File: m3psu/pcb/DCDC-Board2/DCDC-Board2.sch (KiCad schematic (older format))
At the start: 6 parts

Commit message: Start DC/DC routing
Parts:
- gave numbers to parts that had none: 6
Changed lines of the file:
@@
 EESchema Schematic File Version 2
 LIBS:agg-kicad
-LIBS:m3psu-cache
 EELAYER 25 0
 EELAYER END
 $Descr A4 11693 8268
 encoding utf-8
-Sheet 8 13
+Sheet 1 3
 Title ""
 Date ""
@@
 ~ALERT
 $Comp
-L GND #PWR?
+L GND #PWR01
 U 1 1 56E23B16
 P 9150 1700
-F 0 "#PWR?" H 9020 1740 50  0001 L CNN
+F 0 "#PWR01" H 9020 1740 50  0001 L CNN
 F 1 "GND" H 9150 1600 50  0000 C CNN
 F 2 "" H 9150 1700 60  0000 C CNN
@@
 $EndComp
 $Comp
-L GND #PWR?
+L GND #PWR02
 U 1 1 56E23B1C
 P 8750 1700
-F 0 "#PWR?" H 8620 1740 50  0001 L CNN
+F 0 "#PWR02" H 8620 1740 50  0001 L CNN
 F 1 "GND" H 8750 1600 50  0000 C CNN
 F 2 "" H 8750 1700 60  0000 C CNN
@@
 $EndComp
 $Comp
-L GND #PWR?
+L GND #PWR03
 U 1 1 56E23B22
 P 8750 700
-F 0 "#PWR?" H 8620 740 50  0001 L CNN
+F 0 "#PWR03" H 8620 740 50  0001 L CNN
 F 1 "GND" H 8750 600 50  0000 C CNN
 F 2 "" H 8750 700 60  0000 C CNN
@@
 $EndComp
 $Comp
-L GND #PWR?
+L GND #PWR04
 U 1 1 56E23B28
 P 9150 700
-F 0 "#PWR?" H 9020 740 50  0001 L CNN
+F 0 "#PWR04" H 9020 740 50  0001 L CNN
 F 1 "GND" H 9150 600 50  0000 C CNN
 F 2 "" H 9150 700 60  0000 C CNN
@@
 $EndComp
 $Comp
-L GND #PWR?
+L GND #PWR05
 U 1 1 56E23B2E
 P 10150 1700
-F 0 "#PWR?" H 10020 1740 50  0001 L CNN
+F 0 "#PWR05" H 10020 1740 50  0001 L CNN
 F 1 "GND" H 10150 1600 50  0000 C CNN
 F 2 "" H 10150 1700 60  0000 C CNN
@@
 $EndComp
 $Comp
-L GND #PWR?
+L GND #PWR06
 U 1 1 56E23B34
 P 10550 1700
-F 0 "#PWR?" H 10420 1740 50  0001 L CNN
+F 0 "#PWR06" H 10420 1740 50  0001 L CNN
 F 1 "GND" H 10550 1600 50  0000 C CNN
 F 2 "" H 10550 1700 60  0000 C CNN
@@
 $EndComp
 $Comp
-L GND #PWR?
+L GND #PWR07
 U 1 1 56E23B3A
 P 10150 700
-F 0 "#PWR?" H 10020 740 50  0001 L CNN
+F 0 "#PWR07" H 10020 740 50  0001 L CNN
 F 1 "GND" H 10150 600 50  0000 C CNN
 F 2 "" H 10150 700 60  0000 C CNN
@@
 $EndComp
 $Comp
-L GND #PWR?
+L GND #PWR08
 U 1 1 56E23B40
 P 10550 700
-F 0 "#PWR?" H 10420 740 50  0001 L CNN
+F 0 "#PWR08" H 10420 740 50  0001 L CNN
 F 1 "GND" H 10550 600 50  0000 C CNN
 F 2 "" H 10550 700 60  0000 C CNN
@@
 CAN+
 $Comp
-L GND #PWR?
+L GND #PWR09
 U 1 1 56E23B52
 P 9150 3000
-F 0 "#PWR?" H 9020 3040 50  0001 L CNN
+F 0 "#PWR09" H 9020 3040 50  0001 L CNN
 F 1 "GND" H 9150 2900 50  0000 C CNN
 F 2 "" H 9150 3000 60  0000 C CNN
@@
 $EndComp
 $Comp
-L GND #PWR?
+L GND #PWR010
 U 1 1 56E23B58
 P 8750 3000
-F 0 "#PWR?" H 8620 3040 50  0001 L CNN
+F 0 "#PWR010" H 8620 3040 50  0001 L CNN
 F 1 "GND" H 8750 2900 50  0000 C CNN
 F 2 "" H 8750 3000 60  0000 C CNN
@@
 $EndComp
 $Comp
-L GND #PWR?
+L GND #PWR011
 U 1 1 56E23B5E
 P 8750 2000
-F 0 "#PWR?" H 8620 2040 50  0001 L CNN
+F 0 "#PWR011" H 8620 2040 50  0001 L CNN
 F 1 "GND" H 8750 1900 50  0000 C CNN
 F 2 "" H 8750 2000 60  0000 C CNN
@@
 $EndComp
 $Comp
-L GND #PWR?
+L GND #PWR012
 U 1 1 56E23B64
 P 9150 2000
-F 0 "#PWR?" H 9020 2040 50  0001 L CNN
+F 0 "#PWR012" H 9020 2040 50  0001 L CNN
 F 1 "GND" H 9150 1900 50  0000 C CNN
 F 2 "" H 9150 2000 60  0000 C CNN
@@
 PYRO1
 $Comp
-L GND #PWR?
+L GND #PWR013
 U 1 1 56E23B86
 P 10150 3000
-F 0 "#PWR?" H 10020 3040 50  0001 L CNN
+F 0 "#PWR013" H 10020 3040 50  0001 L CNN
 F 1 "GND" H 10150 2900 50  0000 C CNN
 F 2 "" H 10150 3000 60  0000 C CNN
@@
 $EndComp
 $Comp
-L GND #PWR?
+L GND #PWR014
 U 1 1 56E23B8C
 P 10550 3000
-F 0 "#PWR?" H 10420 3040 50  0001 L CNN
+F 0 "#PWR014" H 10420 3040 50  0001 L CNN
 F 1 "GND" H 10550 2900 50  0000 C CNN
 F 2 "" H 10550 3000 60  0000 C CNN
@@
 $EndComp
 $Comp
-L GND #PWR?
+L GND #PWR015
 U 1 1 56E23B92
 P 10150 2000
-F 0 "#PWR?" H 10020 2040 50  0001 L CNN
+F 0 "#PWR015" H 10020 2040 50  0001 L CNN
 F 1 "GND" H 10150 1900 50  0000 C CNN
 F 2 "" H 10150 2000 60  0000 C CNN
@@
 $EndComp
 $Comp
-L GND #PWR?
+L GND #PWR016
 U 1 1 56E23B98
 P 10550 2000
-F 0 "#PWR?" H 10420 2040 50  0001 L CNN
+F 0 "#PWR016" H 10420 2040 50  0001 L CNN
 F 1 "GND" H 10550 1900 50  0000 C CNN
 F 2 "" H 10550 2000 60  0000 C CNN
@@
 INTERCONNECTS
 $Comp
-L GND #PWR?
+L GND #PWR017
 U 1 1 56E23BAF
 P 9600 4000
-F 0 "#PWR?" H 9470 4040 50  0001 L CNN
+F 0 "#PWR017" H 9470 4040 50  0001 L CNN
 F 1 "GND" H 9600 3900 50  0000 C CNN
 F 2 "" H 9600 4000 60  0000 C CNN
@@
 	8800 1550 8700 1550
 $Comp
-L PWR #FLG?
+L PWR #FLG018
 U 1 1 56E23C21
 P 9600 3950
-F 0 "#FLG?" H 9600 4110 50  0001 C CNN
+F 0 "#FLG018" H 9600 4110 50  0001 C CNN
 F 1 "PWR" H 9600 4040 50  0000 C CNN
 F 2 "" H 9600 3950 50  0001 C CNN
@@
 	9600 3950 9600 4000
 $Comp
-L CONN_02x10 J?
+L CONN_02x10 J1
 U 1 1 56E23C29
 P 9000 750
-F 0 "J?" H 8900 850 50  0000 L CNN
+F 0 "J1" H 8900 850 50  0000 L CNN
 F 1 "WEST TOP" H 8950 -250 50  0000 C CNN
 F 2 "agg:TFML-110-02-L-D" H 9000 750 50  0001 C CNN
@@
 $EndComp
 $Comp
-L CONN_02x10 J?
+L CONN_02x10 J4
 U 1 1 56E23C31
 P 10400 750
-F 0 "J?" H 10300 850 50  0000 L CNN
+F 0 "J4" H 10300 850 50  0000 L CNN
 F 1 "EAST TOP" H 10350 -250 50  0000 C CNN
 F 2 "agg:TFML-110-02-L-D" H 10400 750 50  0001 C CNN
@@
 $EndComp
 $Comp
-L CONN_02x10 J?
+L CONN_02x10 J2
 U 1 1 56E23C39
 P 9000 2050
-F 0 "J?" H 8900 2150 50  0000 L CNN
+F 0 "J2" H 8900 2150 50  0000 L CNN
 F 1 "WEST BOT" H 8950 1050 50  0000 C CNN
 F 2 "agg:SFML-110-02-L-D-LC" H 9000 2050 50  0001 C CNN
@@
 $EndComp
 $Comp
-L CONN_02x10 J?
+L CONN_02x10 J5
 U 1 1 56E23C41
 P 10400 2050
-F 0 "J?" H 10300 2150 50  0000 L CNN
+F 0 "J5" H 10300 2150 50  0000 L CNN
 F 1 "EAST BOT" H 10350 1050 50  0000 C CNN
 F 2 "agg:SFML-110-02-L-D-LC" H 10400 2050 50  0001 C CNN
@@
 $EndComp
 $Comp
-L CONN_02x05 J?
+L CONN_02x05 J3
 U 1 1 56E23C48
 P 9000 3300
-F 0 "J?" H 8900 3400 50  0000 L CNN
+F 0 "J3" H 8900 3400 50  0000 L CNN
 F 1 "NORTH TOP" H 8950 2800 50  0000 C CNN
 F 2 "agg:SFML-105-02-L-D" H 9000 3300 50  0001 C CNN
@@
 ~ALERT
 $Comp
-L CONN_02x05 J?
+L CONN_02x05 J6
 U 1 1 56E23C63
 P 10400 3300
-F 0 "J?" H 10300 3400 50  0000 L CNN
+F 0 "J6" H 10300 3400 50  0000 L CNN
 F 1 "NORTH BOT" H 10350 2800 50  0000 C CNN
 F 2 "agg:SFML-105-02-L-D-LC" H 10400 3300 50  0001 C CNN
@@
 V_MAIN
 $Comp
-L VCC #PWR?
+L VCC #PWR019
 U 1 1 56E23C7F
 P 9050 4050
-F 0 "#PWR?" H 9050 4160 50  0001 L CNN
+F 0 "#PWR019" H 9050 4160 50  0001 L CNN
 F 1 "VCC" V 9000 4150 50  0000 C CNN
 F 2 "" H 9050 4050 60  0000 C CNN
@@
 	8900 4050 9050 4050
 $Comp
-L 3v3 #PWR?
+L 3v3 #PWR020
 U 1 1 56E23C86
 P 10450 4050
-F 0 "#PWR?" H 10450 4160 50  0001 L CNN
+F 0 "#PWR020" H 10450 4160 50  0001 L CNN
 F 1 "3v3" V 10400 4150 50  0000 C CNN
 F 2 "" H 10450 4050 60  0000 C CNN
@@
 3v3_PSU
 $Comp
-L PWR #FLG?
+L PWR #FLG021
 U 1 1 56E23C8E
 P 9000 4000
-F 0 "#FLG?" H 9000 4160 50  0001 C CNN
+F 0 "#FLG021" H 9000 4160 50  0001 C CNN
 F 1 "PWR" H 9000 4090 50  0000 C CNN
 F 2 "" H 9000 4000 50  0001 C CNN
@@
 Connection ~ 9000 4050
 $Comp
-L PWR #FLG?
+L PWR #FLG022
 U 1 1 56E23C96
 P 10400 4000
-F 0 "#FLG?" H 10400 4160 50  0001 C CNN
+F 0 "#FLG022" H 10400 4160 50  0001 C CNN
 F 1 "PWR" H 10400 4090 50  0000 C CNN
 F 2 "" H 10400 4000 50  0001 C CNN

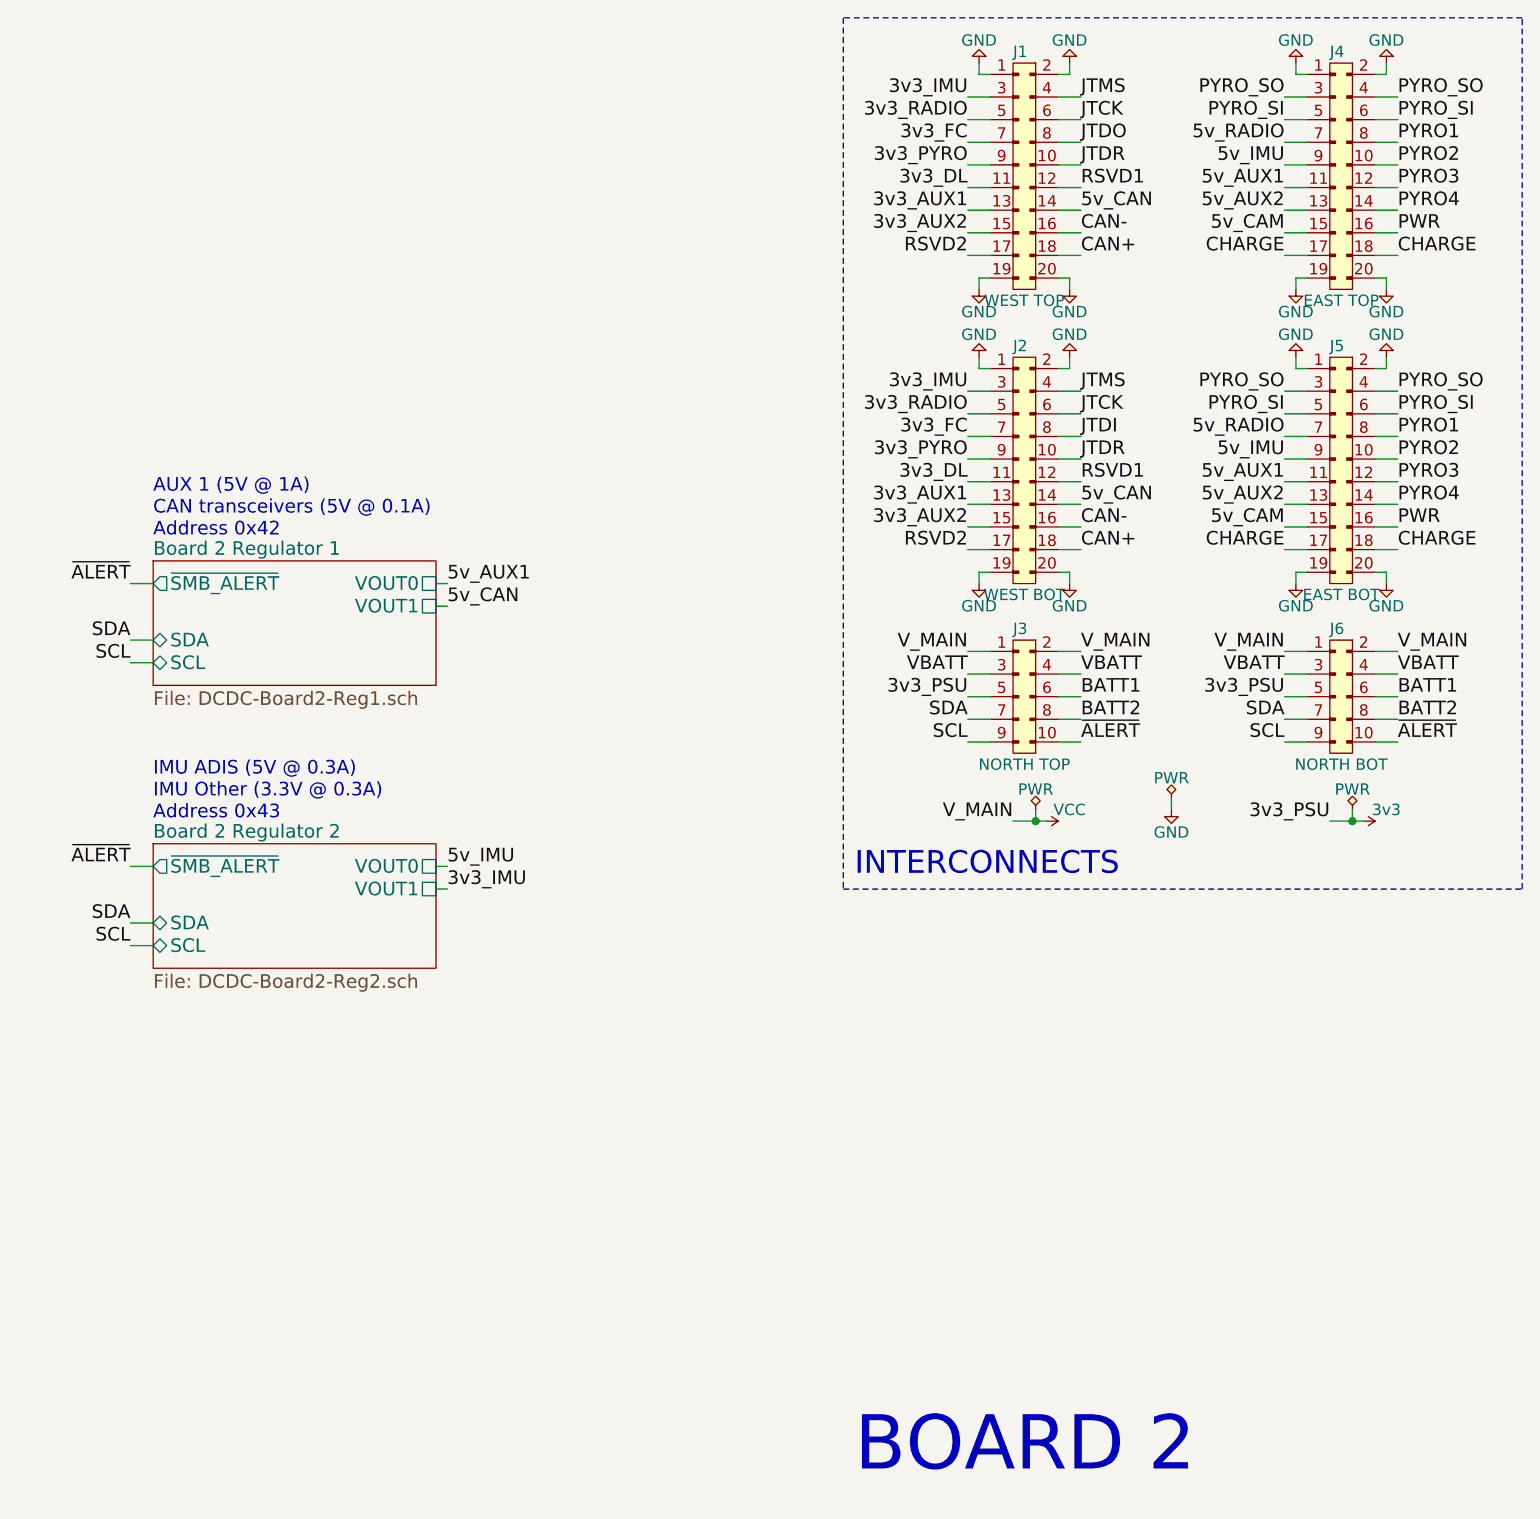
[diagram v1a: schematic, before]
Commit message: Finish routing DC-DC Board 2
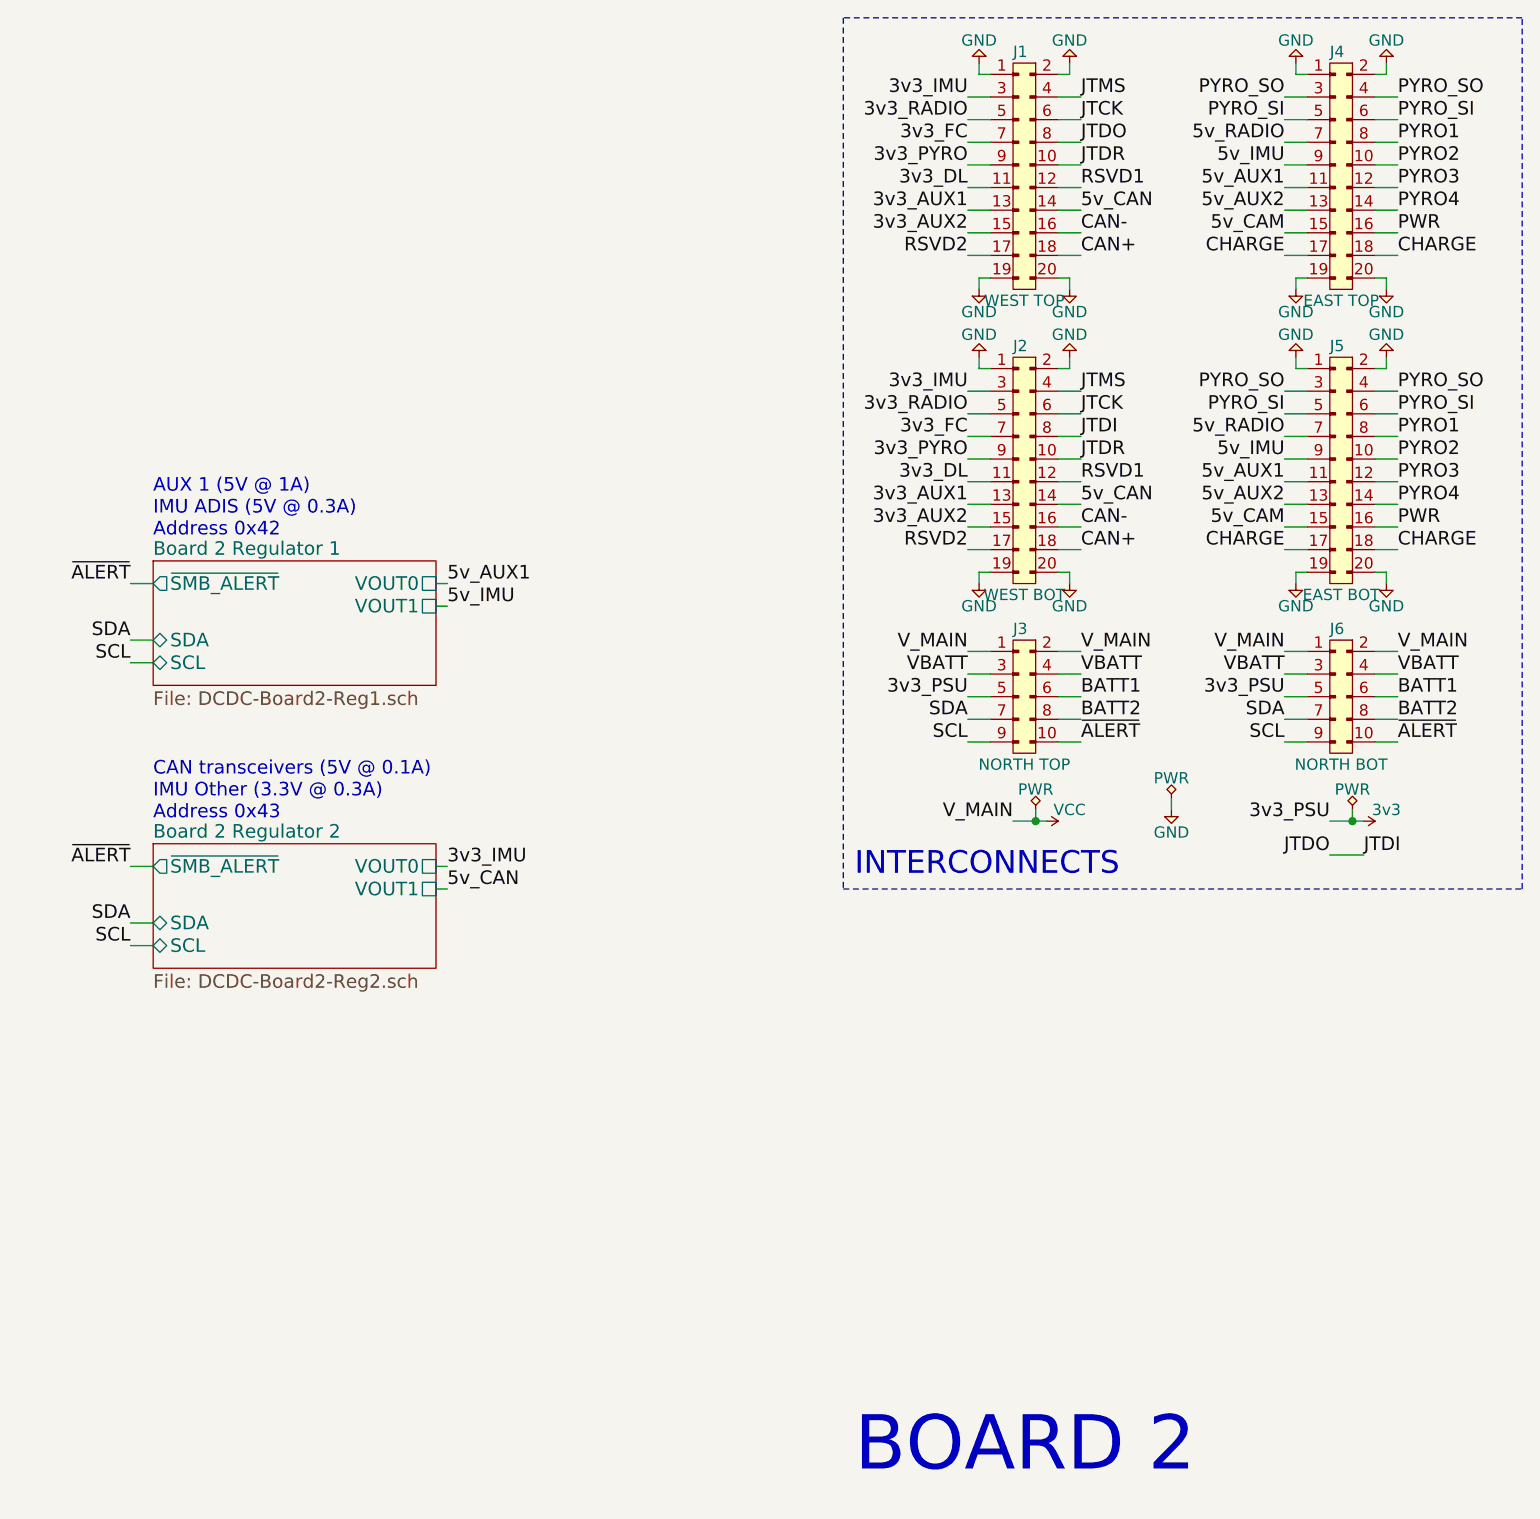
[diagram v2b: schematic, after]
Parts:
- J3: footprint agg:SFML-105-02-L-D -> agg:TFML-105-02-L-D
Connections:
- net JTDO is gone; now on net JTDI: J1.8
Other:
- note added: "AUX 1 (5V @ 1A)\nIMU ADIS (5V @ 0.3A)\nAddress 0x42"
- note added: "CAN transceivers (5V @ 0.1A)\nIMU Other (3.3V @ 0.3A)\nAddress 0x43"
- note removed: "AUX 1 (5V @ 1A)\nCAN transceivers (5V @ 0.1A)\nAddress 0x42"
- note removed: "IMU ADIS (5V @ 0.3A)\nIMU Other (3.3V @ 0.3A)\nAddress 0x43"
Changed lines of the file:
@@
 EESchema Schematic File Version 2
 LIBS:agg-kicad
+LIBS:DCDC-Board2-cache
 EELAYER 25 0
 EELAYER END
@@
 $EndDescr
 Text Notes 5100 2800 0    60   ~ 0
-AUX 1 (5V @ 1A)\nCAN transceivers (5V @ 0.1A)\nAddress 0x42
+AUX 1 (5V @ 1A)\nIMU ADIS (5V @ 0.3A)\nAddress 0x42
 Text Notes 5100 4050 0    60   ~ 0
-IMU ADIS (5V @ 0.3A)\nIMU Other (3.3V @ 0.3A)\nAddress 0x43
+CAN transceivers (5V @ 0.1A)\nIMU Other (3.3V @ 0.3A)\nAddress 0x43
 Text Notes 8200 6950 0    240  ~ 0
 BOARD 2
@@
 Text Label 6400 3000 0    60   ~ 0
 5v_AUX1
-Text Label 6400 3100 0    60   ~ 0
+Text Label 6400 4350 0    60   ~ 0
 5v_CAN
 Wire Wire Line
@@
 Wire Wire Line
 	5100 4600 5000 4600
-Text Label 6400 4350 0    60   ~ 0
+Text Label 6400 4250 0    60   ~ 0
 3v3_IMU
-Text Label 6400 4250 0    60   ~ 0
+Text Label 6400 3100 0    60   ~ 0
 5v_IMU
 Wire Wire Line
@@
 F 0 "J3" H 8900 3400 50  0000 L CNN
 F 1 "NORTH TOP" H 8950 2800 50  0000 C CNN
-F 2 "agg:SFML-105-02-L-D" H 9000 3300 50  0001 C CNN
+F 2 "agg:TFML-105-02-L-D" H 9000 3300 50  0001 C CNN
 F 3 "" H 9000 3300 50  0001 C CNN
 	1    9000 3300
@@
 	10400 4000 10400 4050
 Connection ~ 10400 4050
+Wire Wire Line
+	10300 4200 10450 4200
+Text Label 10450 4200 0    60   ~ 0
+JTDI
+Text Label 10300 4200 2    60   ~ 0
+JTDO
 $EndSCHEMATC

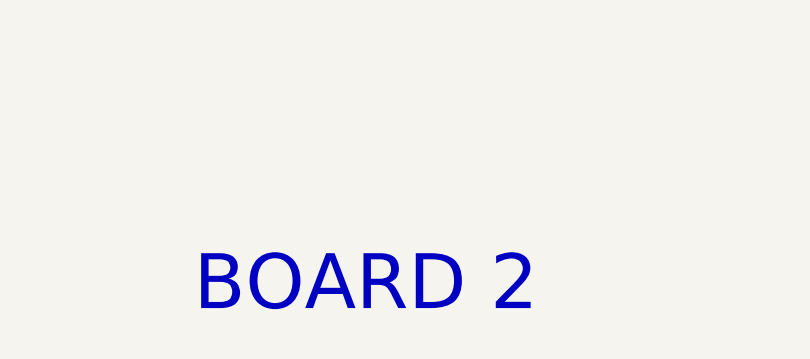
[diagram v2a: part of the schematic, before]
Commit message: Add schematic properties to dc/dc 2
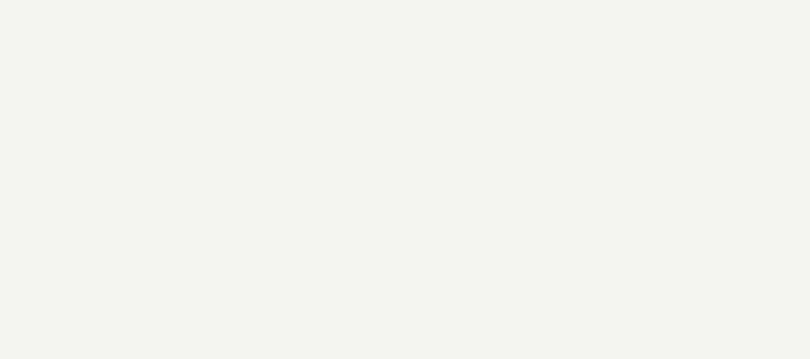
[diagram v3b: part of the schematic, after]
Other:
- note removed: "BOARD 2"
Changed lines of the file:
@@
 encoding utf-8
 Sheet 1 3
-Title ""
-Date ""
-Rev ""
-Comp ""
-Comment1 ""
+Title "M3PSU - DC/DC Converter Board 2"
+Date "2016-06-28"
+Rev "1"
+Comp "CU Spaceflight"
+Comment1 "Drawn by: Levin Tan, Jamie Wood"
 Comment2 ""
 Comment3 ""
@@
 Text Notes 5100 4050 0    60   ~ 0
 CAN transceivers (5V @ 0.1A)\nIMU Other (3.3V @ 0.3A)\nAddress 0x43
-Text Notes 8200 6950 0    240  ~ 0
-BOARD 2
 $Sheet
 S 5100 2900 1250 550
